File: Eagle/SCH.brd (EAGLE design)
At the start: 75.4 x 45.4 mm, 22 parts, among them Q1 IRF540, Q2 IRF540, Q3 IRF540, U1 ARDUINO-NANO

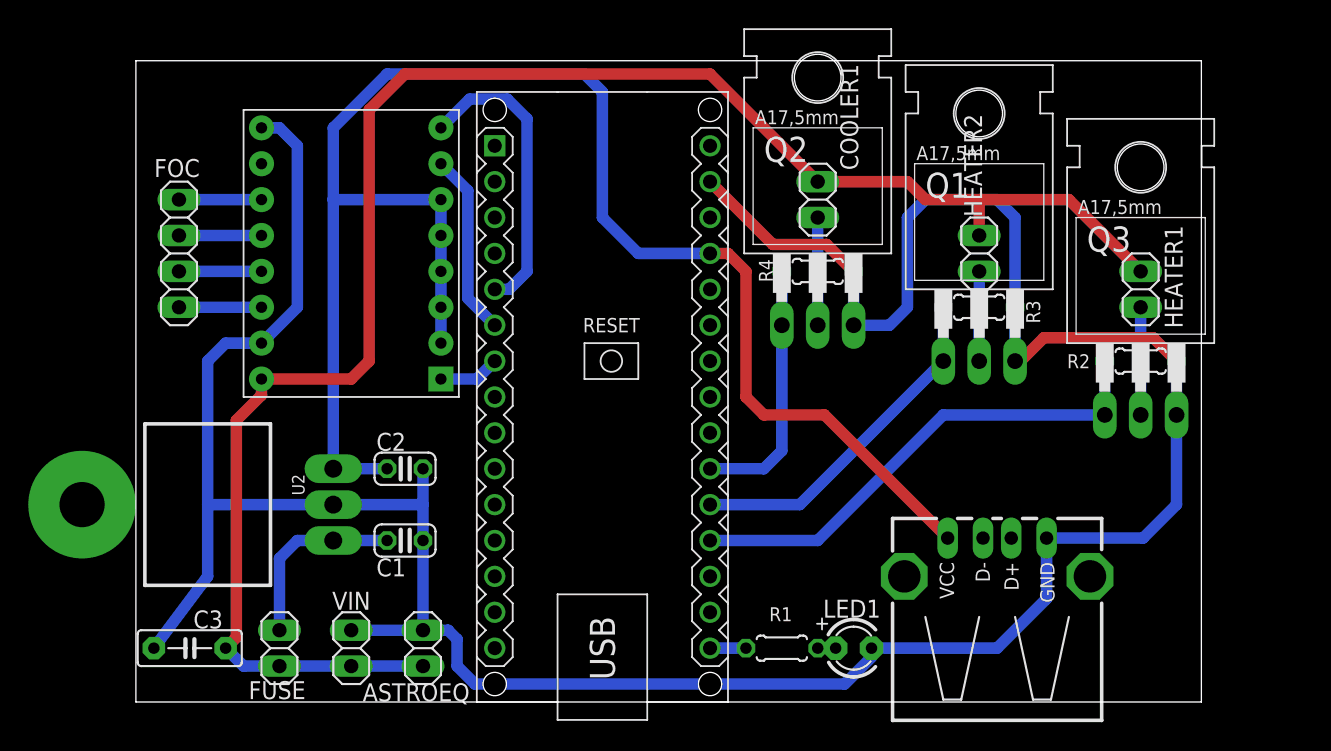
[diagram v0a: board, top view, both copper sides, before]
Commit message: Added photos, Arduino SW update
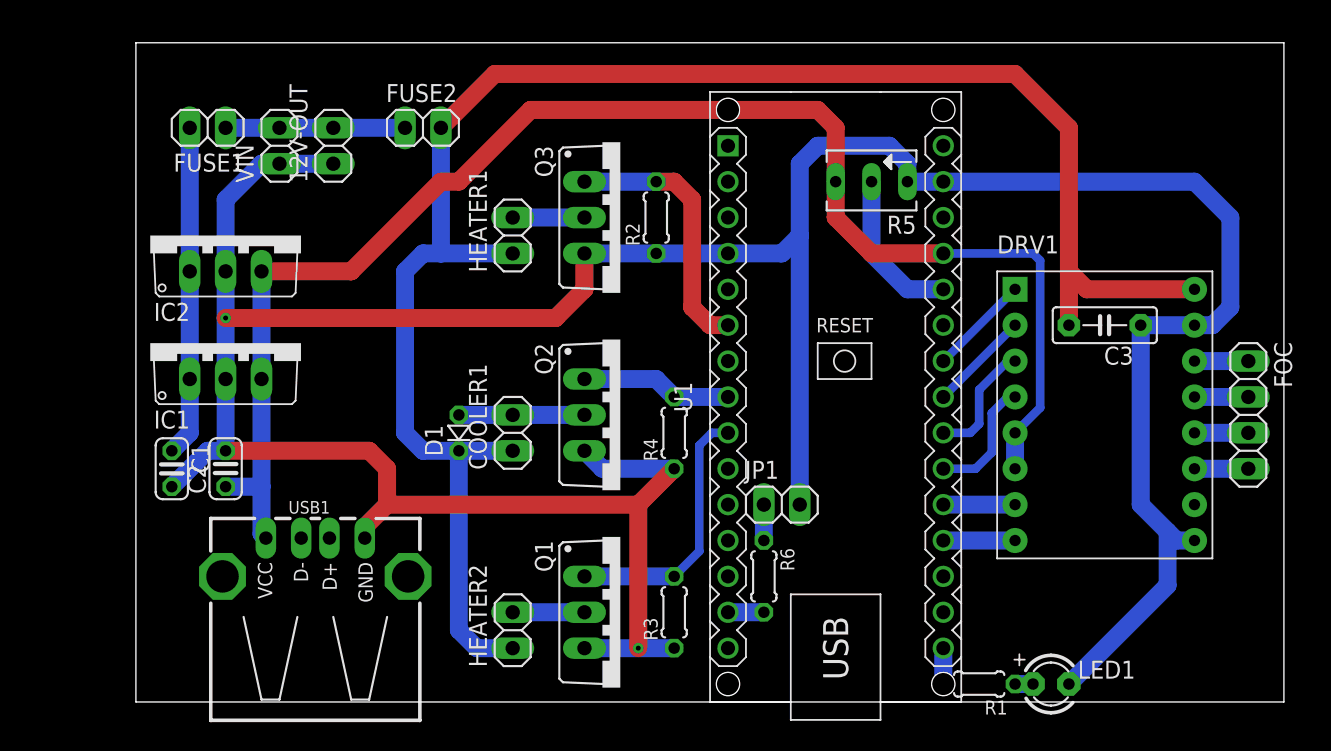
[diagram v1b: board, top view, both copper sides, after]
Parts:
- removed ASTROEQ, FUSE: (no value), pinhead:1X02
- removed U2: (no value), Seeed-IC:TO-220
- added 12V-OUT, FUSE1, FUSE2, JP1: (no value), pinhead:1X02
- added D1: (no value), diode:D-2.5
- added IC1, IC2: L7805, linear:TO220V
- added R5: (no value), pot:B64Y
- added R6: 220R, resistor:0204/5
- LED1: device Adafruit:LED3MM -> adafruit:LED3MM
- Q1, Q2, Q3: device transistor-fet:TO220 -> transistor-power:TO220BV
- moved FOC 76.6 mm to (78.7, 20.3), turned to 270 degrees
- moved C3 68.7 mm to (68.6, 26.7), turned to 180 degrees
- moved USB1 48.3 mm to (12.7, 8.89)
- moved HEATER1 44.6 mm to (26.7, 33.0), turned to 90 degrees
- moved HEATER2 42.4 mm to (26.7, 5.08), turned to 90 degrees
- moved DRV1 39.1 mm to (61.0, 30.5), turned to 0 degrees
- moved Q3 37.6 mm to (34.3, 34.3), turned to 270 degrees
- moved VIN 35.9 mm to (10.2, 39.4), turned to 90 degrees
- moved R2 35.8 mm to (36.8, 34.3), turned to 90 degrees
- moved Q1 35.0 mm to (34.3, 6.35), turned to 270 degrees
- moved R3 30.5 mm to (38.1, 6.35), turned to 90 degrees
- moved COOLER1 27.2 mm to (26.7, 19.1), turned to 90 degrees
- moved Q2 18.9 mm to (34.3, 20.3), turned to 270 degrees
- moved C1 17.3 mm to (2.54, 16.5), turned to 270 degrees
- moved U1 16.5 mm to (49.5, 21.6)
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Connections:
- net N$17 renamed D13
- removed net GND.1: U1.J1.4
- removed net N$7: Q2.1, R4.2, U1.J2.10
- new net D3: Q3.G, R2.2, U1.J1.6
- new net D5: Q2.G, R4.2, U1.J1.8
- new net D6: Q1.G, R3.2, U1.J1.9
- new net N$17: DRV1.M2, U1.J2.10
- new net N$18: DRV1.M1, U1.J2.9
- new net N$19: JP1.1, R6.1
- new net N$20: DRV1.M0, U1.J2.8
- new net N$8: 12V-OUT.2, FUSE1.1, FUSE2.1, VIN.2
- net +12V: now also D1.C, FUSE2.2; no longer ASTROEQ.2, FUSE.1, VIN.2
- net +5V: now also IC1.3, IC2.3, R5.A; no longer DRV1.M0, DRV1.M1, DRV1.M2, U2.3
- net GND: now also 12V-OUT.1, IC1.2, IC2.2, JP1.2, Q1.S, Q2.S, Q3.S, R5.E, U1.J1.4; no longer ASTROEQ.1, Q1.3, Q2.3, Q3.3, U2.2, U2.HEAT
- net N$10: now also Q1.D; no longer Q1.2
- net N$11: now also Q3.D; no longer Q3.2
- net N$12: now also DRV1.STEP, U1.J2.11; no longer DRV1.ENABLE, U1.J1.7
- net N$2: now also R5.S, U1.J2.5; no longer DRV1.DIR, U1.J1.5
- net N$3: now also R6.2, U1.J1.14; no longer DRV1.STEP, U1.J1.6
- net N$4: now also FUSE1.2, IC1.1, IC2.1; no longer FUSE.2, U2.1
- net N$5: now also DRV1.DIR; no longer Q3.1, R2.2
- net N$6: now also DRV1.ENABLE, U1.J2.7; no longer Q1.1, R3.2, U1.J2.11
- net N$9: now also D1.A, Q2.D; no longer Q2.2
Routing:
- net GND: track 209.0 -> 240.6 mm, vias 0 -> 2
- net N$5: track 35.4 -> 5.08 mm
- net D3: track 0.00 -> 18.8 mm
- net D6: track 0.00 -> 18.8 mm
- net N$7: track 18.3 -> 0.00 mm
- net N$6: track 24.5 -> 7.18 mm
- net N$8: track 0.00 -> 12.7 mm
- net D5: track 0.00 -> 10.7 mm
- net N$3: track 13.0 -> 2.54 mm
- net N$4: track 13.2 -> 23.4 mm
- net N$2: track 21.1 -> 11.2 mm
- net +5V: track 114.8 -> 105.0 mm
- net N$17: track 0.00 -> 8.82 mm
- net N$18: track 0.00 -> 8.60 mm
- net N$20: track 0.00 -> 7.18 mm
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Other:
- board size 75.4 x 45.4 mm -> 81.3 x 46.7 mm

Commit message: New PCB design
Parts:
- removed COOLER1, HEATER1, HEATER2: (no value), pinhead:1X02
- removed FOC: (no value), pinhead:1X04
- removed U1: ARDUINO-NANO, DIY:ARDUINO-NANO-3.0
- added JP2: FOCUSER, pinhead:1X04
- added JP3, JP4, JP5: (no value), SparkFun-Connectors:SCREWTERMINAL-5MM-2
- added U$1: NANO, Arduino-clone:NANO
- FUSE1: value (none) -> 1.5A; device pinhead:1X02 -> fuse:FUSE_HOLDER_5X20MM
- FUSE2: value (none) -> 2A; device pinhead:1X02 -> fuse:FUSE_HOLDER_5X20MM
- VIN: device pinhead:1X02 -> SparkFun-Connectors:SCREWTERMINAL-5MM-2
- moved FUSE2 71.1 mm to (-41.9, 6.35), turned to 270 degrees
- moved 12V-OUT 60.8 mm to (-40.6, 12.7), turned to 180 degrees
- moved D1 58.4 mm to (-20.3, -20.3), turned to 0 degrees
- moved USB1 57.6 mm to (-36.2, -21.6)
- moved FUSE1 49.4 mm to (-30.5, 6.35), turned to 270 degrees
- moved Q2 46.8 mm to (-1.27, -10.2)
- moved R5 45.9 mm to (17.8, 6.35)
- moved IC2 45.8 mm to (-19.1, -5.08), turned to 180 degrees
- moved R4 45.5 mm to (3.30, -10.3)
- moved IC1 44.7 mm to (-19.1, -11.4), turned to 180 degrees
- moved C3 44.1 mm to (35.6, -2.54)
- moved DRV1 44.1 mm to (27.9, 1.27)
- moved Q1 44.1 mm to (1.27, -22.9)
- moved Q3 44.1 mm to (1.27, 5.08)
- moved R2 43.1 mm to (5.08, 5.08)
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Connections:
- removed net 3V3: U1.J2.14
- removed net VIN: U1.J2.1
- net +12V: now also JP3.1, JP4.1, JP5.1; no longer COOLER1.1, HEATER1.1, HEATER2.1
- net +5V: now also U$1.5V; no longer U1.J2.4
- net D13: now also U$1.D13; no longer U1.J2.15
- net D3: now also U$1.D3; no longer U1.J1.6
- net D5: now also U$1.D5; no longer U1.J1.8
- net D6: now also U$1.D6; no longer U1.J1.9
- net GND: now also U$1.GND, U$1.GND1; no longer U1.J1.4, U1.J2.2
- net N$10: now also JP4.2; no longer HEATER2.2
- net N$11: now also JP5.2; no longer HEATER1.2
- net N$12: now also U$1.A1; no longer U1.J2.11
- net N$13: now also JP2.1; no longer FOC.1
- net N$14: now also JP2.2; no longer FOC.2
- net N$15: now also JP2.3; no longer FOC.3
- net N$16: now also JP2.4; no longer FOC.4
- net N$17: now also U$1.A2; no longer U1.J2.10
- net N$18: now also U$1.A3; no longer U1.J2.9
- net N$2: now also U$1.A7; no longer U1.J2.5
- net N$20: now also U$1.A4; no longer U1.J2.8
- net N$3: now also U$1.D11; no longer U1.J1.14
- net N$5: now also U$1.A0; no longer U1.J2.12
- net N$6: now also U$1.A5; no longer U1.J2.7
- net N$9: now also JP3.2; no longer COOLER1.2
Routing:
- net +12V: track 124.6 -> 158.6 mm
- net N$9: track 8.89 -> 25.8 mm
- net N$11: track 5.08 -> 22.0 mm
- net N$8: track 12.7 -> 26.7 mm
- net N$4: track 23.4 -> 37.1 mm
- net +5V: track 105.0 -> 117.2 mm
- net GND: track 240.6 -> 249.8 mm, vias 2 -> 1
- net N$10: track 5.08 -> 9.45 mm
- net D5: track 10.7 -> 14.1 mm
- net D6: track 18.8 -> 21.1 mm
- net D3: track 18.8 -> 20.1 mm
- net N$5: track 5.08 -> 3.81 mm
- net N$12: track 5.08 -> 3.81 mm
- net N$1: track 1.27 -> 2.54 mm
- net N$3: track 2.54 -> 3.81 mm
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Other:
- board size 81.3 x 46.7 mm -> 97.8 x 46.7 mm
- board text added: "Arduino Nano"
